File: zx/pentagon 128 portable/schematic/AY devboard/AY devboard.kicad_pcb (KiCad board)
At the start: 2 copper layers, 60 x 68 mm, 15 parts, among them J1 Conn_02x03_Odd_Even, J2 Conn_01x02, J3 AudioJack3, J4 Conn_01x12, U2 YM2149

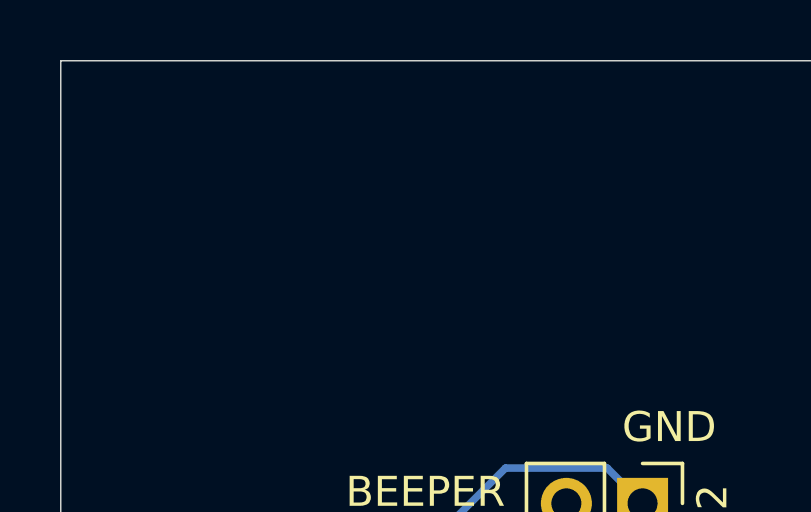
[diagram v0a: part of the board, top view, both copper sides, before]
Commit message: added tape in devboard
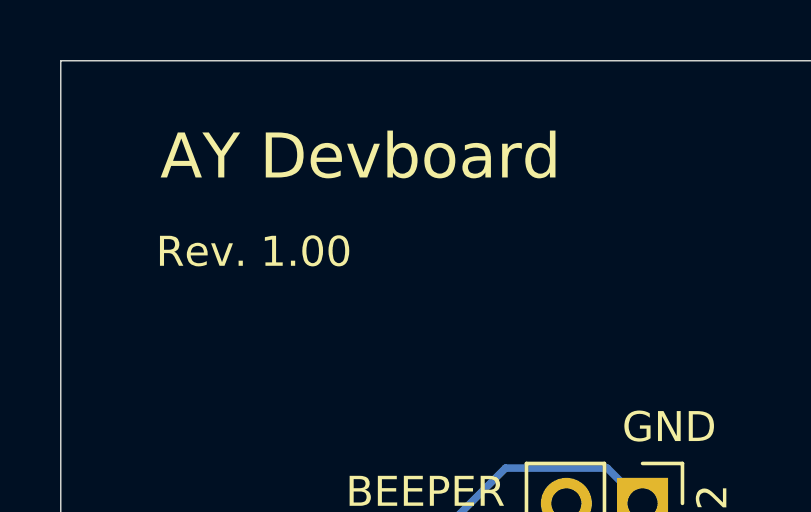
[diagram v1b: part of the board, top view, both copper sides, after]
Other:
- board text added: "AY Devboard"
- board text added: "Rev. 1.00"

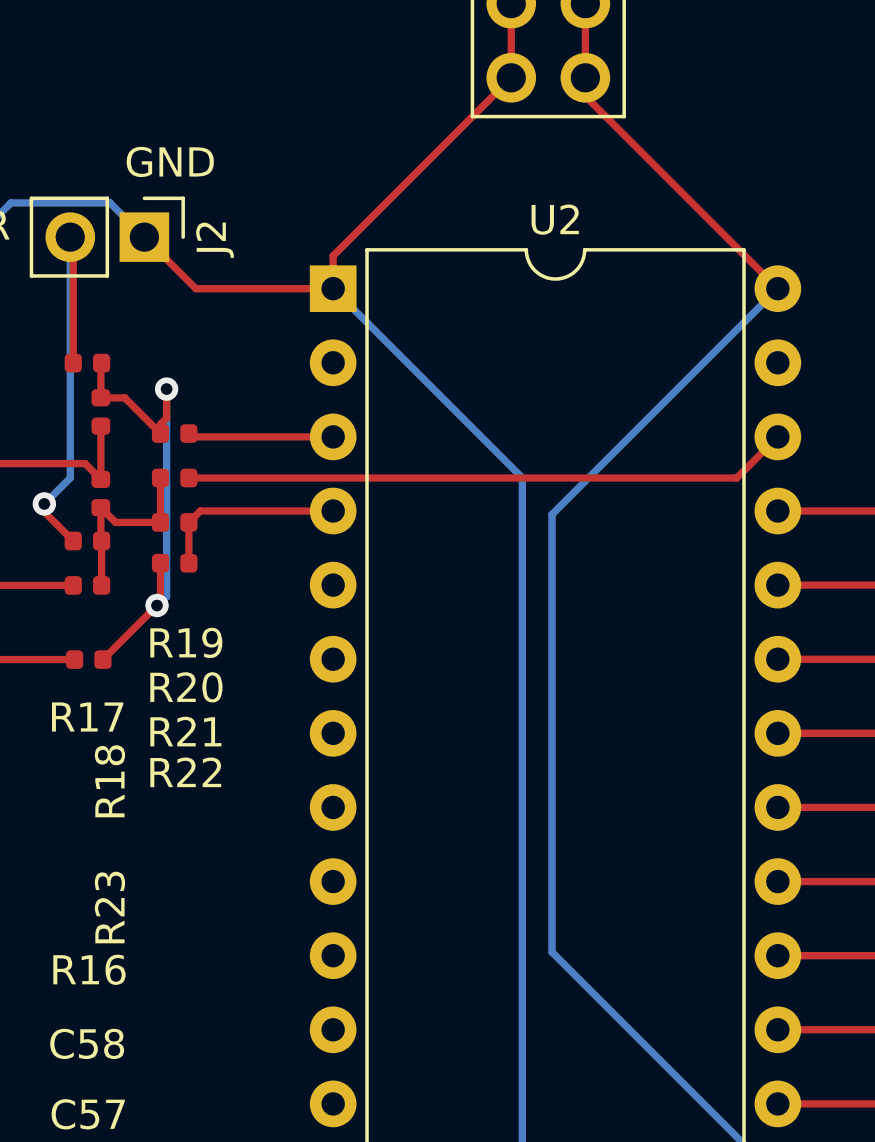
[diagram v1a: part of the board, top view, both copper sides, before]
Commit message: added z80 pdip. updated all boards
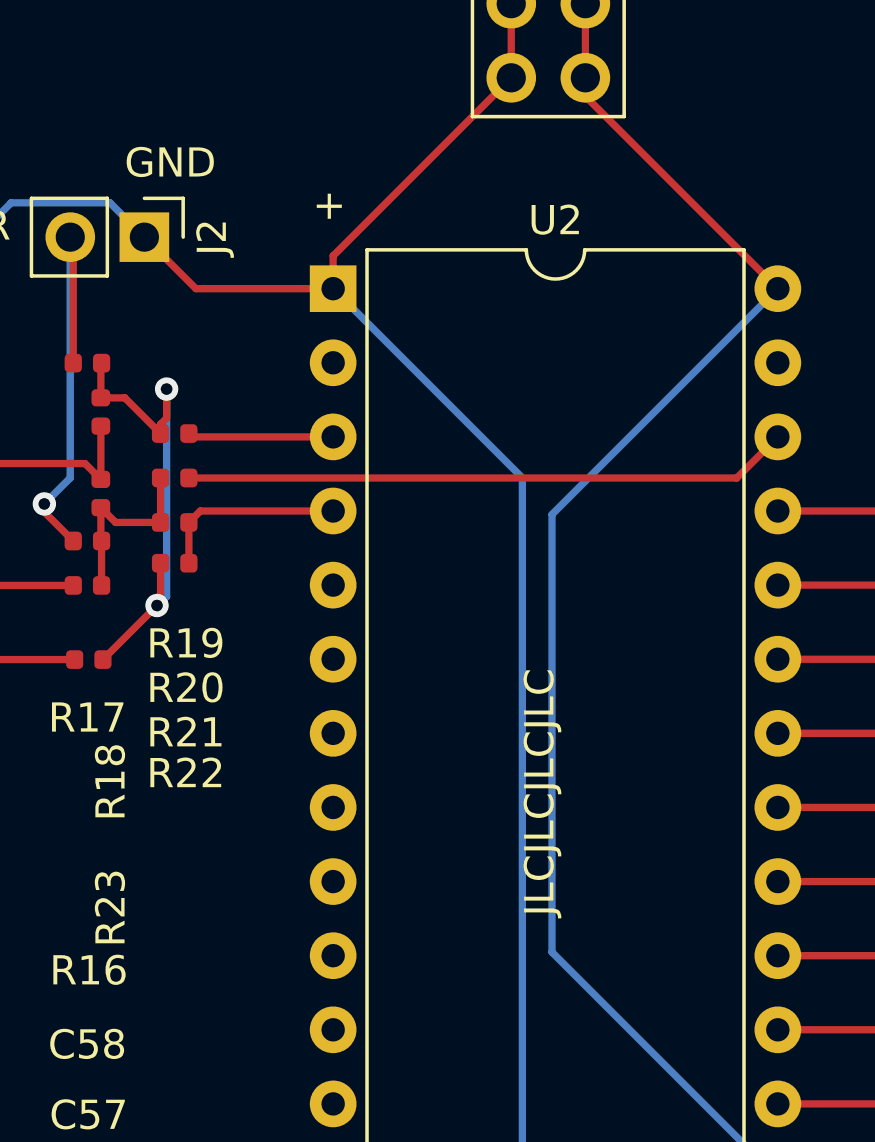
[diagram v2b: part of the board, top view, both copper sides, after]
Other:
- board text added: "+"
- board text added: "JLCJLCJLCJLC"
